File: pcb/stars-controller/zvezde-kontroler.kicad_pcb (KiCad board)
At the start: 2 copper layers, 160 x 100 mm, 33 parts, among them IC1 ATTINY841-SSU, J1 TLC5925, J10 RJ45, J11 RJ45, J12 RJ45, J2 TLC5925, J3 RJ45, J4 RJ45, J5 RJ45, J6 RJ45, J7 RJ45, J8 RJ45, J9 RJ45, P1 CONN_01X08, P2 CONN_01X08, P3 CONN_01X06, P4 CONN_01X08, P5 CONN_01X04, P6 CONN_01X08, P7 CONN_01X04

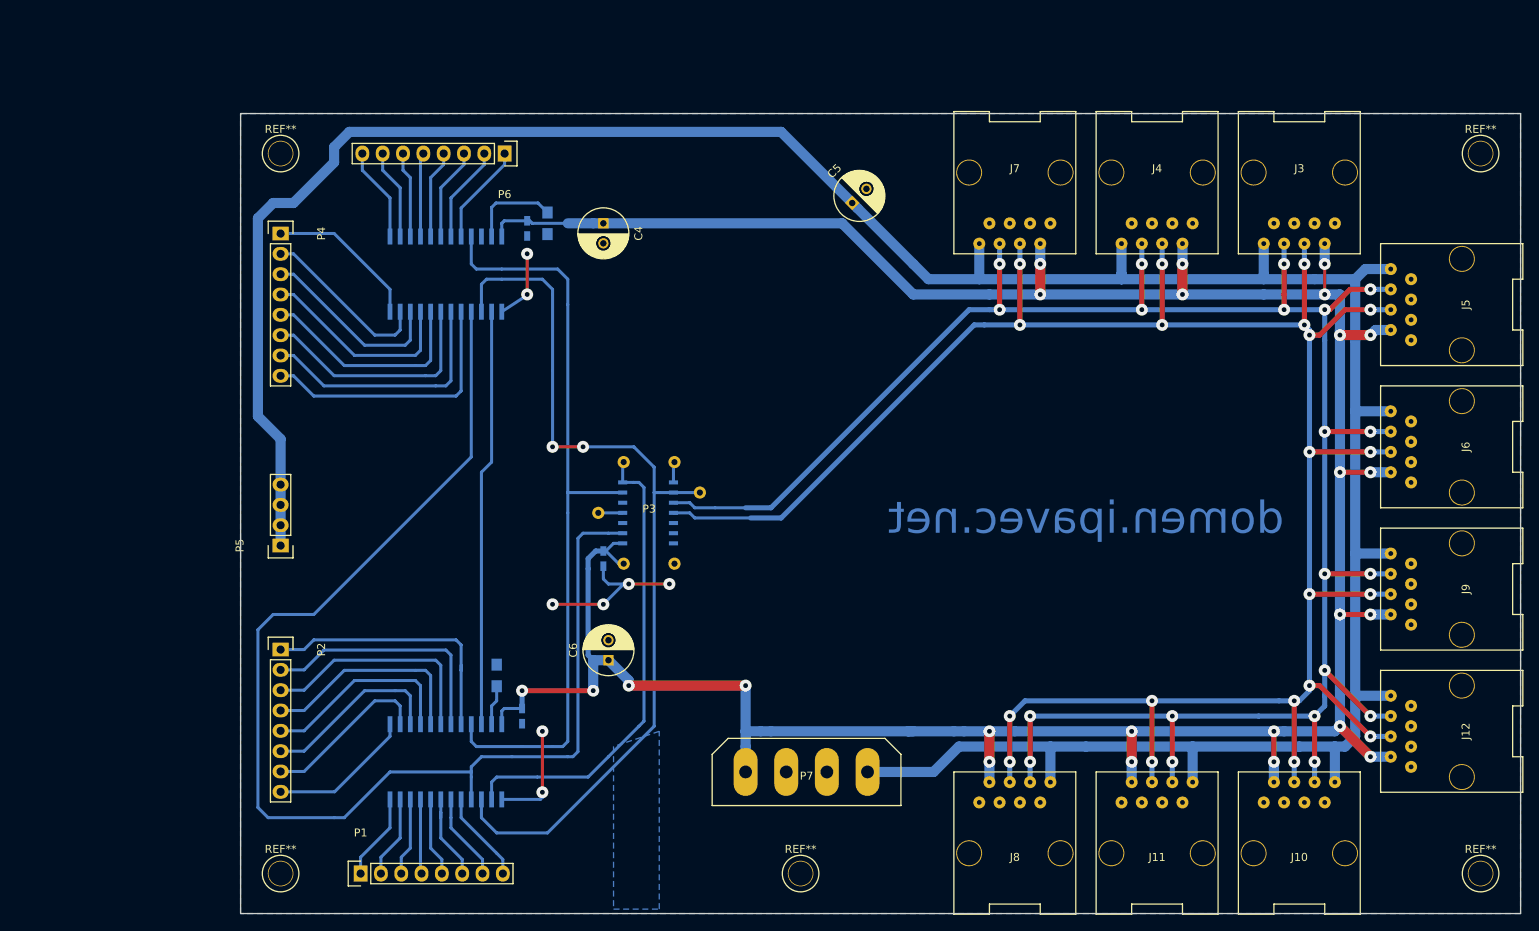
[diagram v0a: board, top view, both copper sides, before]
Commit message: Double sided pcbs
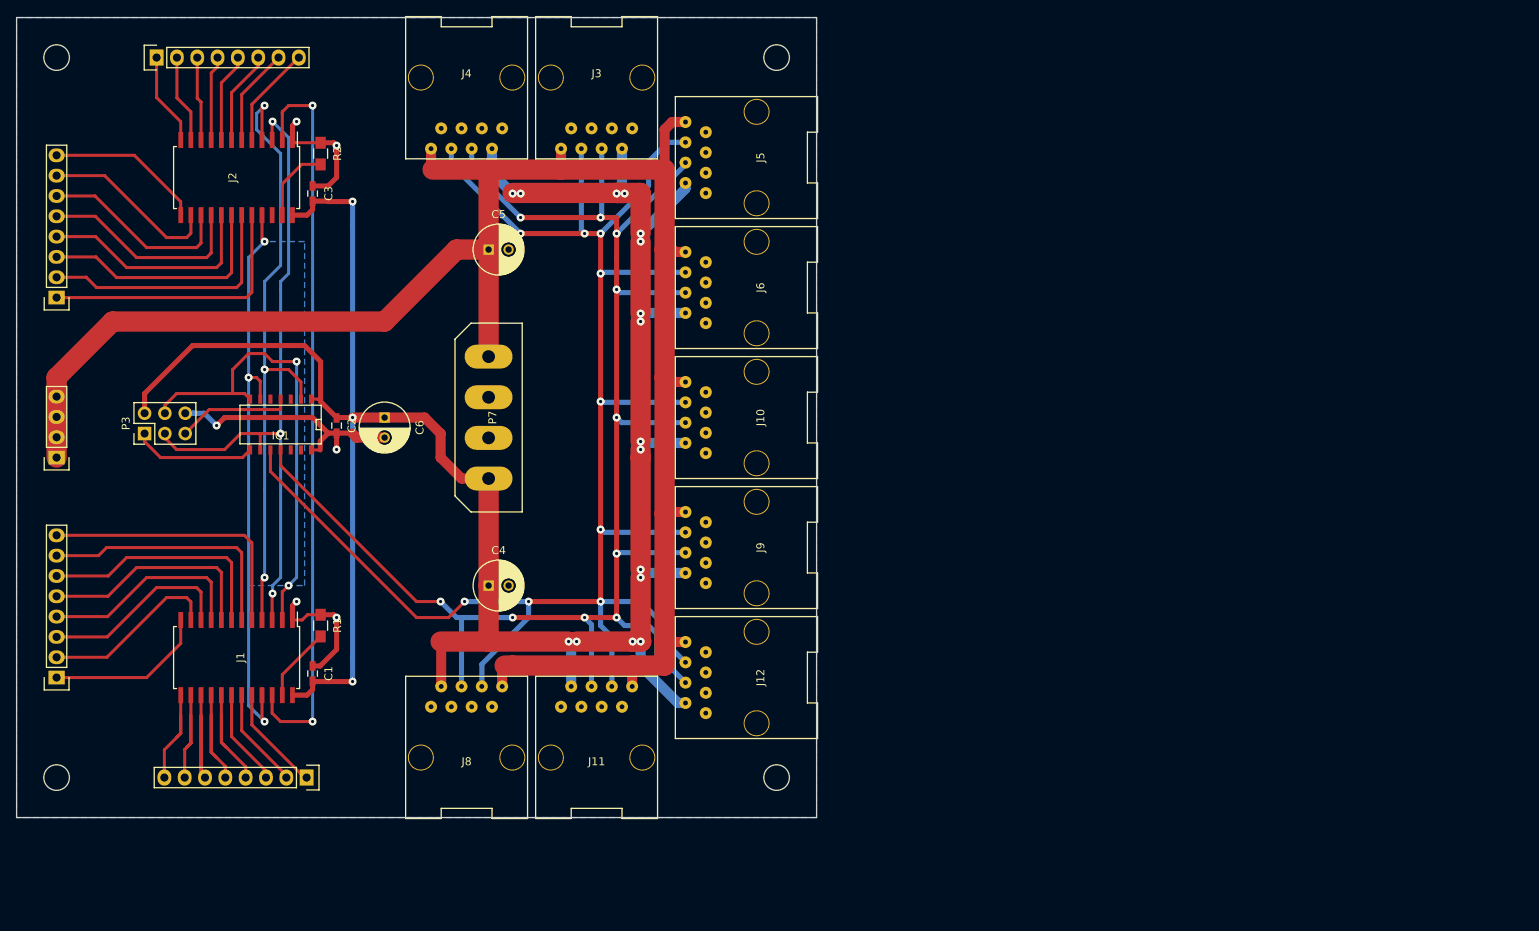
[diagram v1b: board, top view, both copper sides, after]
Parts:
- removed J7: RJ45, rj45:RJ45
- removed the REF** at (118.0, 127.0)
- removed the REF** at (53.0, 37.0)
- removed the REF** at (53.0, 127.0)
- removed the REF** at (203.0, 127.0)
- removed the REF** at (203.0, 37.0)
- added REF**: MountingHole_3.2mm_M3, Mounting_Holes:MountingHole_3.2mm_M3, F.Cu at (115.0, 25.0)
- added REF**: MountingHole_3.2mm_M3, Mounting_Holes:MountingHole_3.2mm_M3, F.Cu at (25.0, 25.0)
- added REF**: MountingHole_3.2mm_M3, Mounting_Holes:MountingHole_3.2mm_M3, F.Cu at (25.0, 115.0)
- added REF**: MountingHole_3.2mm_M3, Mounting_Holes:MountingHole_3.2mm_M3, F.Cu at (115.0, 115.0)
- C1, C2, C3, IC1, J1, J2, R1, R2: moved to F.Cu
- P3: footprint attiny841-spi:ATTINY841-SPI -> Pin_Headers:Pin_Header_Straight_2x03_Pitch2.54mm
- moved J6 90.4 mm to (112.5, 53.8)
- moved J5 90.1 mm to (112.5, 37.5)
- moved J3 88.6 mm to (92.5, 27.5)
- moved J12 88.4 mm to (112.5, 102.5)
- moved J9 88.3 mm to (112.5, 86.2)
- moved J4 87.1 mm to (76.2, 27.5)
- moved J10 87.0 mm to (112.5, 70.0), turned to 90 degrees
- moved J11 71.1 mm to (92.5, 112.5)
- moved J8 69.6 mm to (76.2, 112.5)
- moved P3 63.8 mm to (36.0, 72.0), turned to 90 degrees
- moved P7 59.5 mm to (79.0, 70.0), turned to 90 degrees
- moved P6 58.8 mm to (25.0, 55.0), turned to 90 degrees
- moved C4 47.5 mm to (79.0, 91.0), turned to 0 degrees
- moved IC1 47.3 mm to (53.0, 71.0), turned to 180 degrees
- moved C5 45.8 mm to (79.0, 49.0), turned to 0 degrees
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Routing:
- net +12V: track 359.6 -> 237.1 mm
- net LATCH: track 156.3 -> 78.7 mm, vias 0 -> 3
- net RXD: track 277.5 -> 203.8 mm, vias 20 -> 10
- net +5V: track 379.6 -> 324.3 mm, vias 24 -> 19
- net XCK: track 264.8 -> 221.6 mm, vias 20 -> 9
- net Net-(J1-Pad22): track 52.1 -> 92.6 mm, vias 0 -> 2
- net AVR_SCK: track 114.8 -> 85.2 mm, vias 2 -> 3
- net ENABLE: track 95.7 -> 72.4 mm, vias 0 -> 3
- net Net-(J1-Pad5): track 11.4 -> 34.4 mm
- net GND: track 43.1 -> 65.3 mm, vias 8 -> 6
- net Net-(J2-Pad20): track 12.6 -> 34.3 mm
- net Net-(J1-Pad6): track 10.9 -> 32.2 mm
- net Net-(J2-Pad5): track 33.8 -> 12.8 mm
- net Net-(J2-Pad19): track 12.1 -> 32.3 mm
- net Net-(J1-Pad20): track 33.9 -> 13.6 mm
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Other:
- board size 160 x 100 mm -> 100 x 100 mm
- net class Default: via_dia 1.5 -> 1; via_drill 0.6 -> 0.4
- board text removed: "domen.ipavec.net"
